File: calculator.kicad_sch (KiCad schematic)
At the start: 24 parts, among them J1 USB_B_Micro, J2 Conn_ARM_JTAG_SWD_10, J4 Conn_01x03_Pin, U6 RP2040

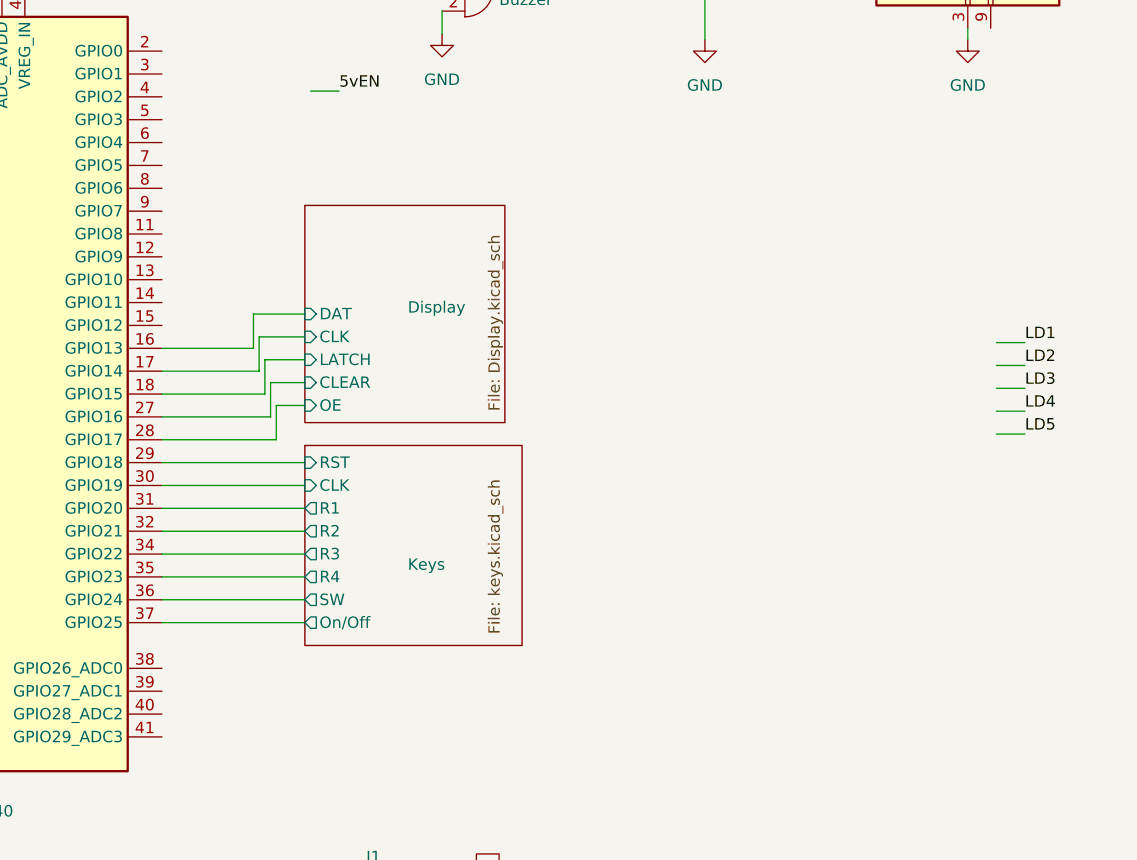
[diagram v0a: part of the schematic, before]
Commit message: Add ROM driver sheet
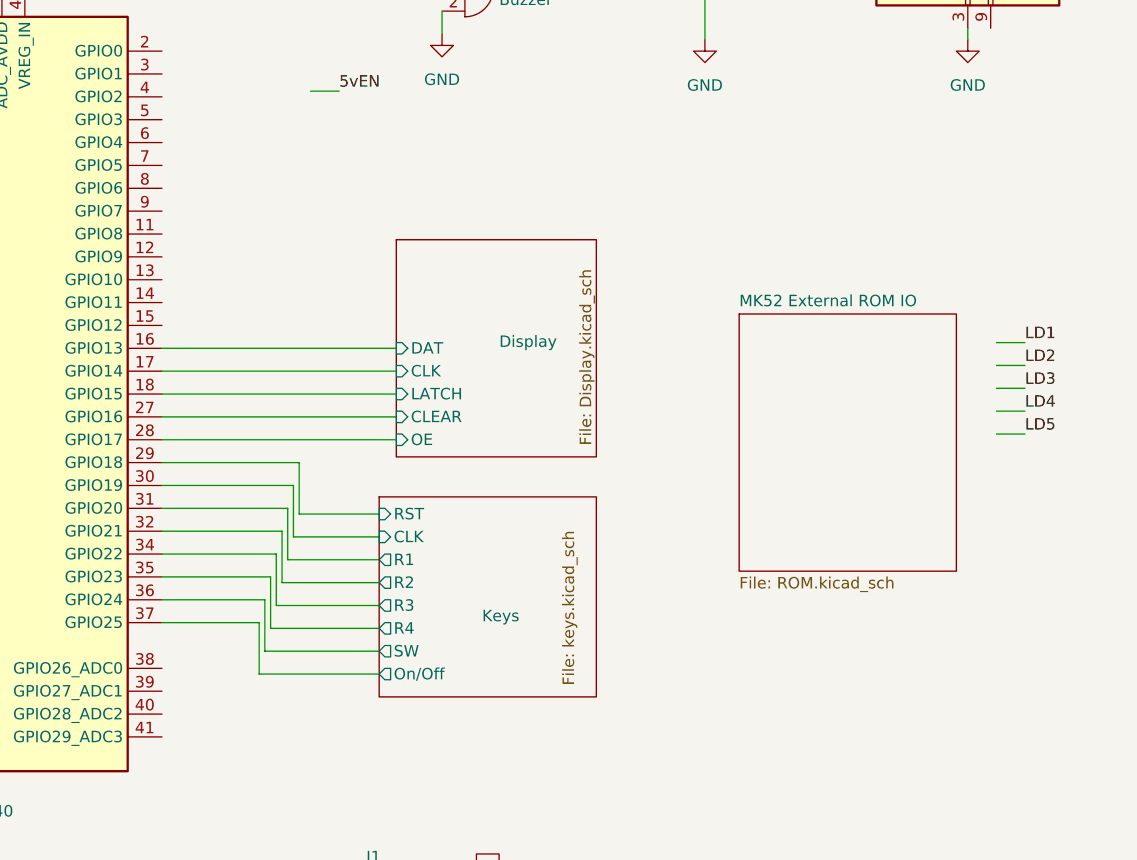
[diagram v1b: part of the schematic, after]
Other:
- added sheet MK52 External ROM IO (ROM.kicad_sch)

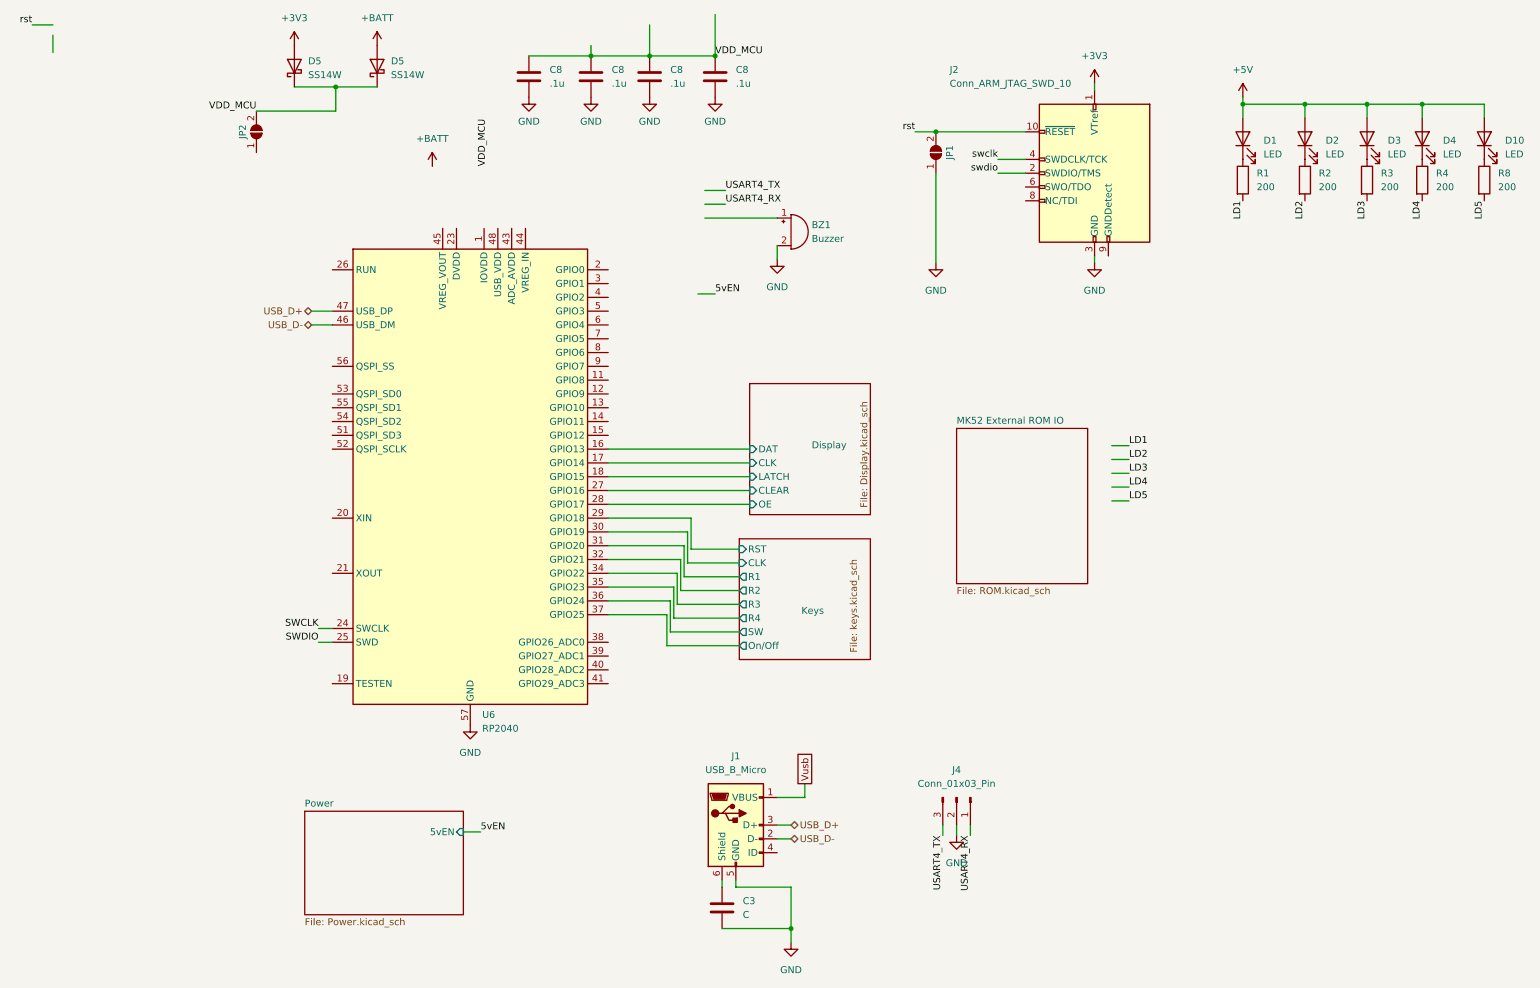
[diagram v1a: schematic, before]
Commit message: Begin screen module
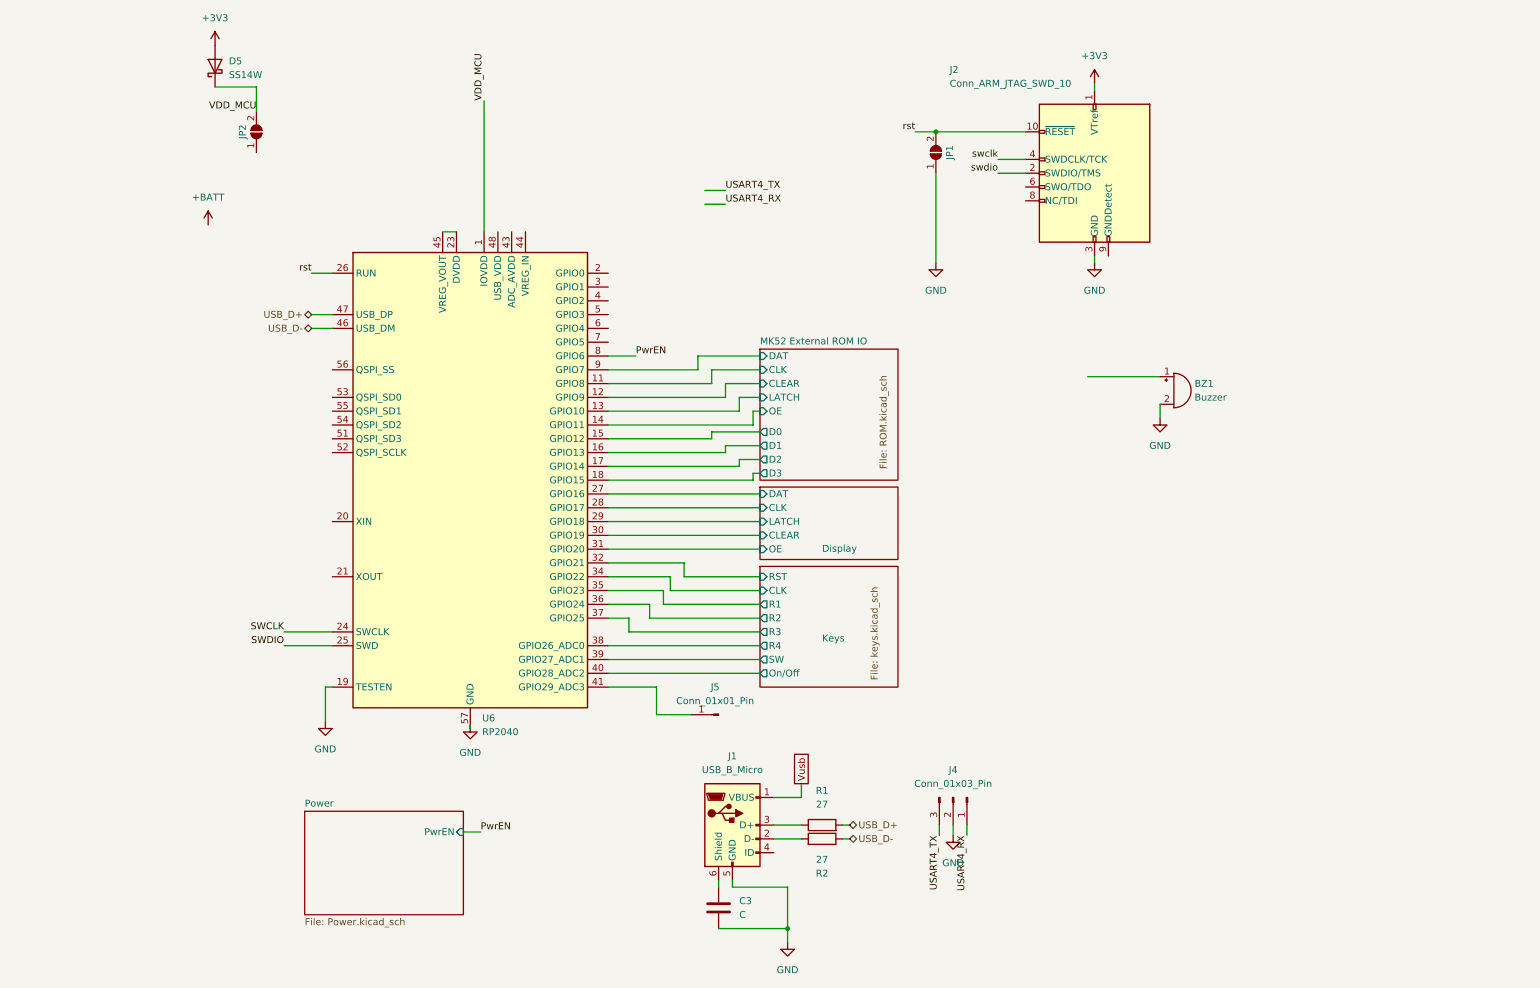
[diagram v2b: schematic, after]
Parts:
- removed C8 (x4): .1u, Capacitor_SMD:C_0603_1608Metric_Pad1.08x0.95mm_HandSolder, symbol Device:C
- removed D1, D10, D2, D3, D4: LED, LED_SMD:LED_0805_2012Metric_Pad1.15x1.40mm_HandSolder, symbol Device:LED
- removed D5: SS14W, Diode_SMD:D_SMA-SMB_Universal_Handsoldering, symbol Device:D_Schottky
- removed R3, R4, R8: 200, Resistor_SMD:R_0603_1608Metric_Pad0.98x0.95mm_HandSolder, symbol Device:R
- added J5: Conn_01x01_Pin, symbol Connector:Conn_01x01_Pin
- R1, R2: value 200 -> 27; footprint Resistor_SMD:R_0603_1608Metric_Pad0.98x0.95mm_HandSolder -> (none)
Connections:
- net LD1 is gone; now on net USB_D+: R1.2
- net Display/CLEAR: now also U6.30 (GPIO19); no longer U6.27 (GPIO16)
- net Display/CLK: now also U6.28 (GPIO17); no longer U6.17 (GPIO14)
- net Display/DAT: now also U6.27 (GPIO16); no longer U6.16 (GPIO13)
- net Display/LATCH: now also U6.29 (GPIO18); no longer U6.18 (GPIO15)
- net Display/OE: now also U6.31 (GPIO20); no longer U6.28 (GPIO17)
- net GND: now also U6.19 (TESTEN)
- net Keys/CLK: now also U6.34 (GPIO22); no longer U6.30 (GPIO19)
- net Keys/On/Off: now also U6.40 (GPIO28_ADC2); no longer U6.37 (GPIO25)
- net Keys/R1: now also U6.35 (GPIO23); no longer U6.31 (GPIO20)
- net Keys/R2: now also U6.36 (GPIO24); no longer U6.32 (GPIO21)
- net Keys/R3: now also U6.37 (GPIO25); no longer U6.34 (GPIO22)
- net Keys/R4: now also U6.38 (GPIO26_ADC0); no longer U6.35 (GPIO23)
- net Keys/RST: now also U6.32 (GPIO21); no longer U6.29 (GPIO18)
- net Keys/SW: now also U6.39 (GPIO27_ADC1); no longer U6.36 (GPIO24)
- net USB_D+: no longer J1.3 (D+)
- net USB_D-: now also R2.1; no longer J1.2 (D-)
- net VDD_MCU: now also U6.1 (IOVDD), U6.10 (IOVDD), U6.22 (IOVDD), U6.33 (IOVDD), U6.42 (IOVDD), U6.49 (IOVDD)
- net rst: now also U6.26 (RUN)
- net MK52 External ROM IO/CLK: now reaches U6.11 (GPIO8)
- net MK52 External ROM IO/CLEAR: now reaches U6.12 (GPIO9)
- net MK52 External ROM IO/LATCH: now reaches U6.13 (GPIO10)
- net MK52 External ROM IO/OE: now reaches U6.14 (GPIO11)
- net MK52 External ROM IO/D0: now reaches U6.15 (GPIO12)
- net at U6.23 (DVDD), U6.50 (DVDD): now also U6.45 (VREG_VOUT)
- net at U6.41 (GPIO29_ADC3): now also J5.1 (Pin_1)
- net PwrEN: now reaches U6.8 (GPIO6)
- net MK52 External ROM IO/DAT: now reaches U6.9 (GPIO7)
- net at R1.1: now also J1.3 (D+)
- net LD2: no longer names the net of R2.2
- net LD2: now also J1.2 (D-)
- new net MK52 External ROM IO/D1: U6.16 (GPIO13)
- new net MK52 External ROM IO/D2: U6.17 (GPIO14)
- new net MK52 External ROM IO/D3: U6.18 (GPIO15)
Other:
- sheet MK52 External ROM IO ports: added CLEAR, CLK, D0, D1, D2, D3, DAT, LATCH, OE; removed none
- sheet Power ports: added PwrEN; removed 5vEN
- moved on the sheet: BZ1, C3, D5, J1, J4, U6
